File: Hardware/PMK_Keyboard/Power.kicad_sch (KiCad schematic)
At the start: 7 parts, among them U301 MIC5528-3.3YMT-T5, U302 MIC5528-3.3YMT-T5

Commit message: Again on hierachic sheet
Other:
- company: (none) -> PumaCorp
- title: (none) -> PMK_Keyboard
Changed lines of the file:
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@@
 (kicad_sch (version 20211123) (generator eeschema)
   (paper "A4")
+  (title_block
+    (title "PMK_Keyboard")
+    (date "2023-02-06")
+    (rev "HW00")
+    (company "PumaCorp")
+    (comment 1 "Design by: NdG")
+  )
   (junction (at 132.08 64.77) (diameter 0) (color 0 0 0 0)
   )

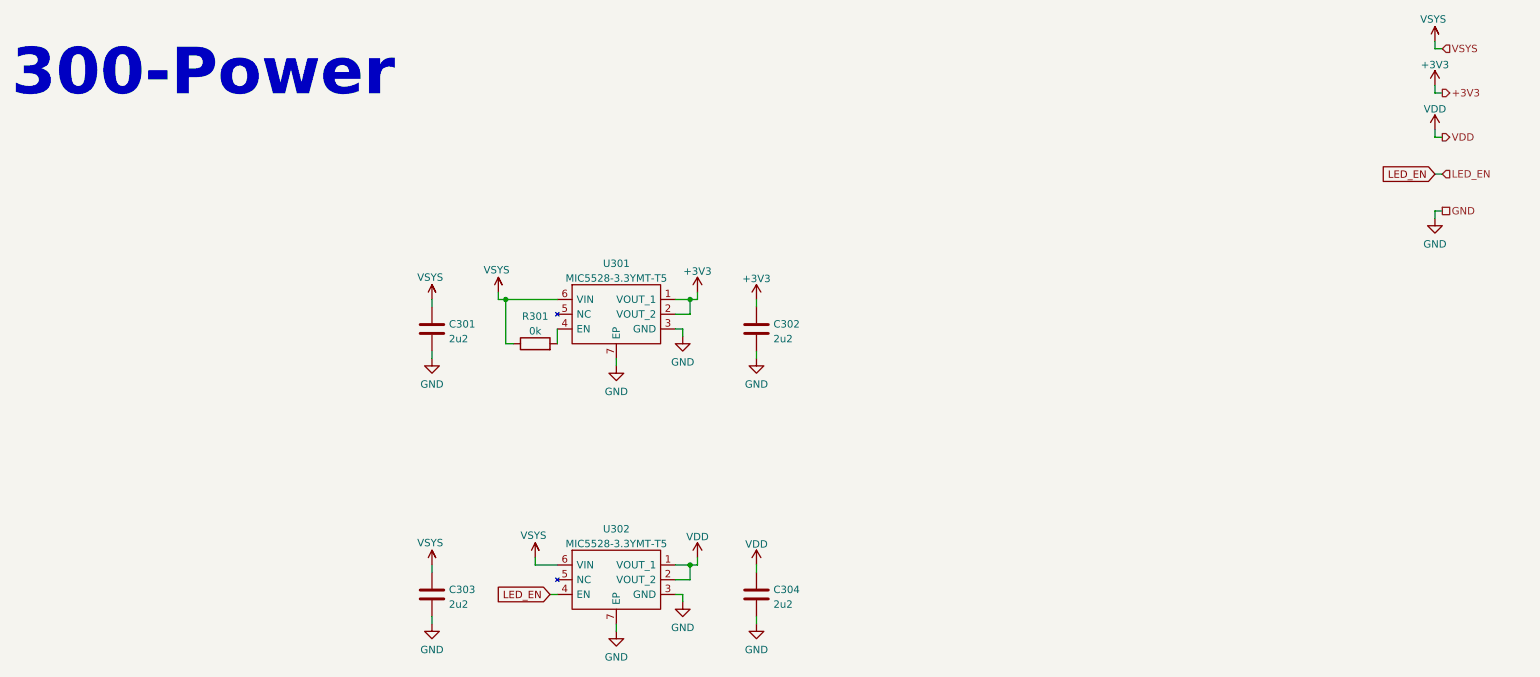
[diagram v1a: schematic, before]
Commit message: Schematic is done, only possible update is change of ESP pins
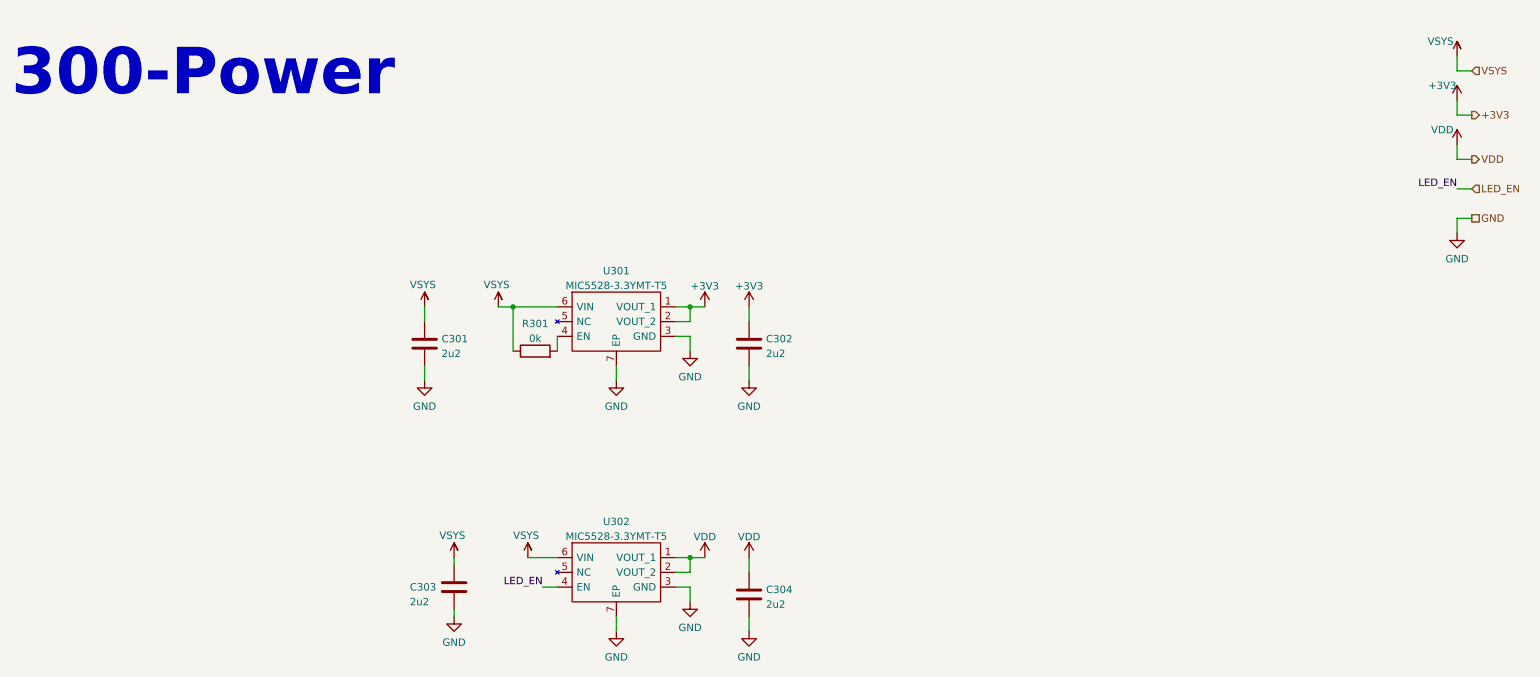
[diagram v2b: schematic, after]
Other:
- moved on the sheet: C301, C302, C303, C304, R301, U301, U302

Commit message: Routing is almost done
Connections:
- net VSYS: now also C301.1, C303.1, R301.1, U301.6 (VIN), U302.6 (VIN)
- net PRIM_LDO_EN: now reaches R301.2, U301.4 (EN)
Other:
- moved on the sheet: C303
